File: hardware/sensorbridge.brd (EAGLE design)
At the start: 55.9 x 53.3 mm, 23 parts

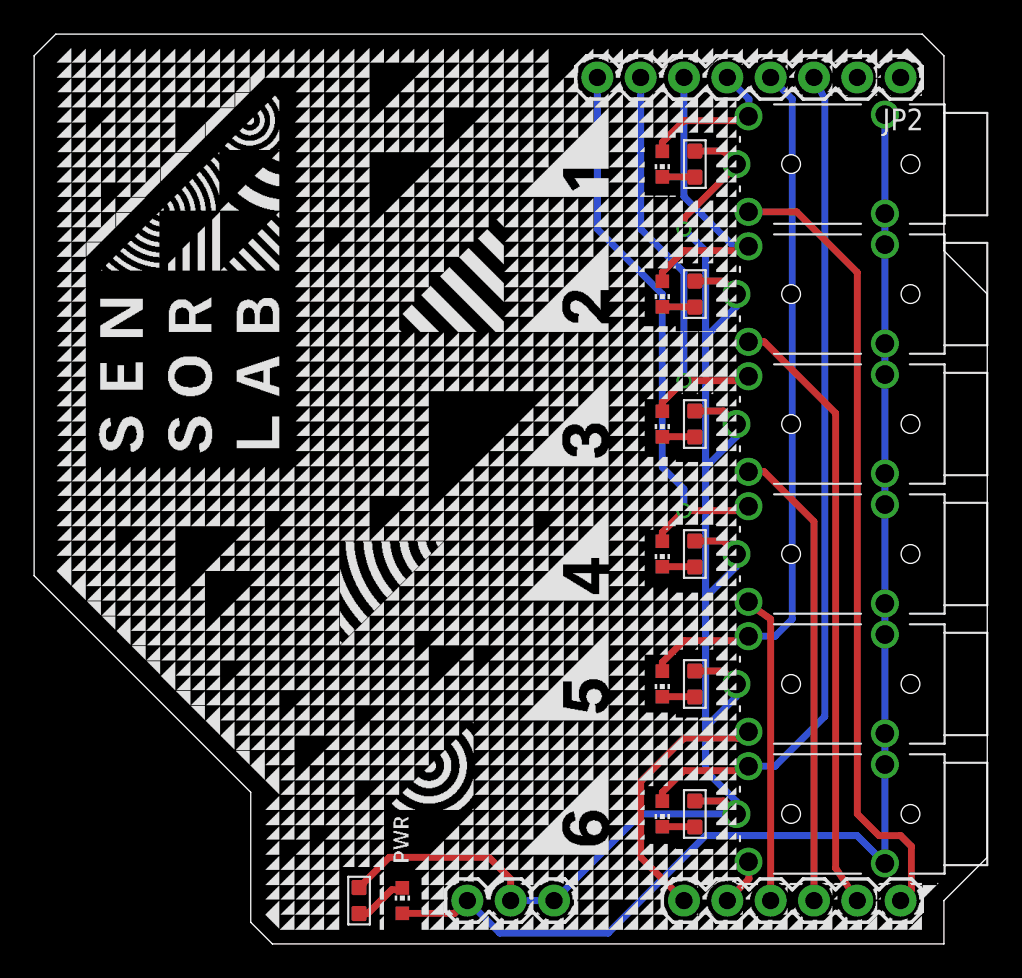
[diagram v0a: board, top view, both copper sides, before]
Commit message: Added ground planes, fixed DRC errors (dirtypcb)
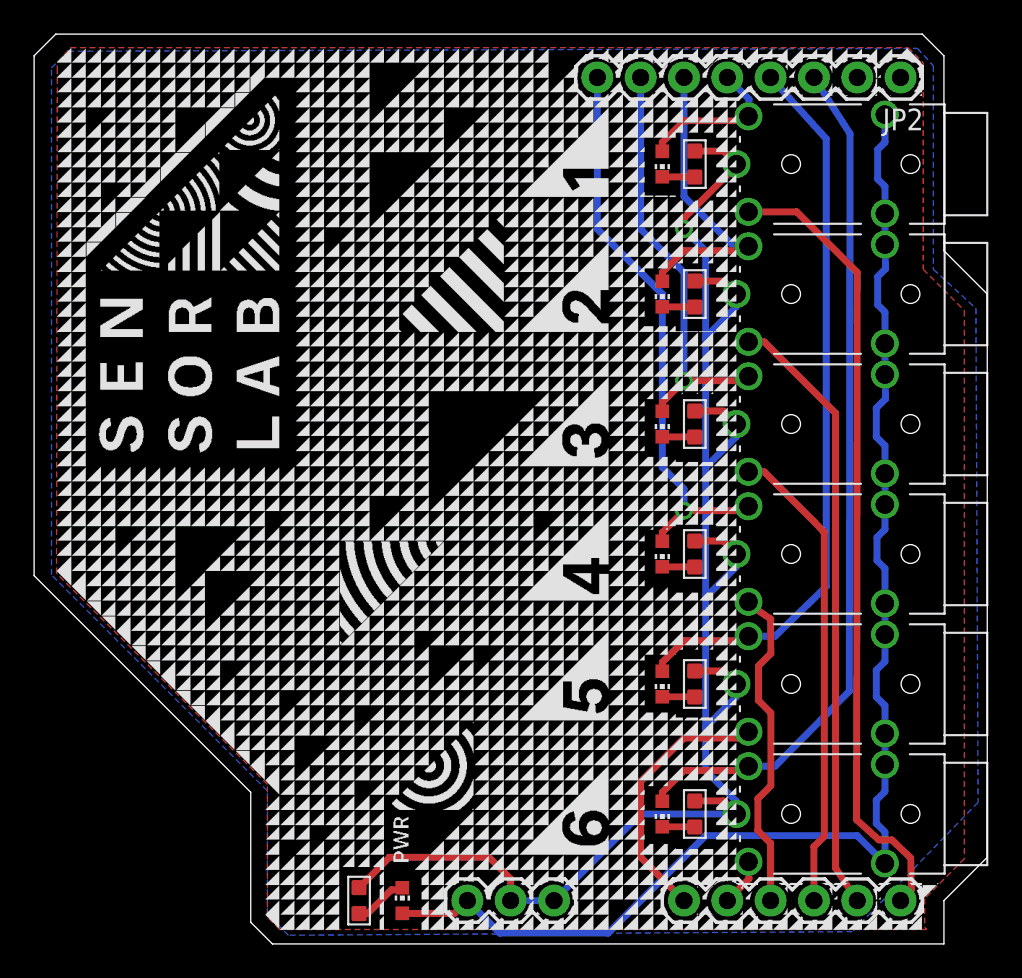
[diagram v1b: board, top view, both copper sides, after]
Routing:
- net +5V: track 76.3 -> 78.7 mm
- net S5_CONN: track 41.5 -> 43.0 mm
- net S4_DATA: track 18.2 -> 19.4 mm
- net S6_CONN: track 49.5 -> 50.6 mm
- added copper zone on layer 1, net GND
- added copper zone on layer 16, net GND

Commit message: Replaced connectors with no-silk versions
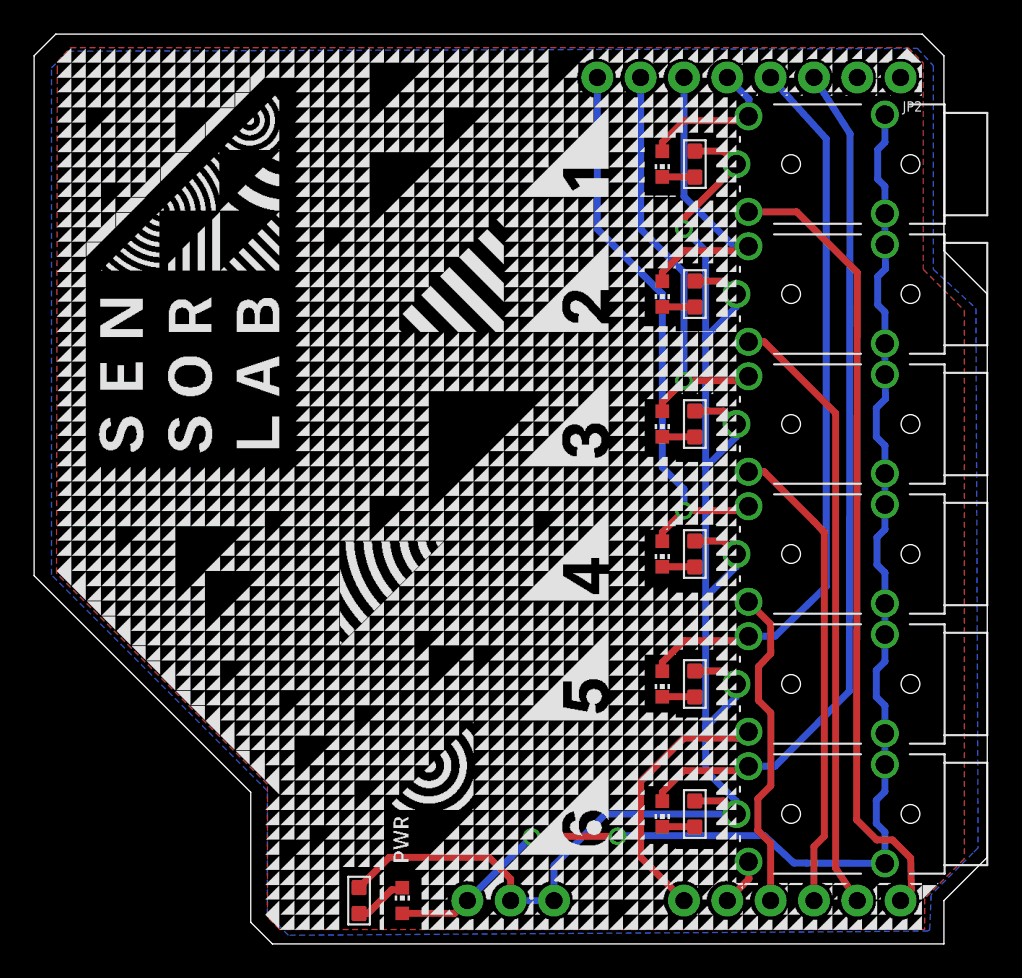
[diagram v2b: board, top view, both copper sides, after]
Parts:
- ANALOG: device SparkFun-Connectors:1X06 -> SparkFun-Connectors:1X06_NO_SILK
- JP2: device SparkFun-Connectors:1X08_ROUND -> SparkFun-Connectors:1X08_NO_SILK
- PWR: device SparkFun-Connectors:1X03 -> SparkFun-Connectors:1X03_NO_SILK
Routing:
- net +5V: track 78.7 -> 77.1 mm, vias 0 -> 2
- net GND: track 97.5 -> 98.7 mm
